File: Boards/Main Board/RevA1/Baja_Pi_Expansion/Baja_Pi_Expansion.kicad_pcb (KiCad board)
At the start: 4 copper layers, 85 x 56 mm, 25 parts, among them J1 Conn_02x10_Counter_Clockwise, J2 Conn_02x12_Counter_Clockwise, J3 Screw_Terminal_01x04, J4 Conn_02x20_Odd_Even, J5 Conn_01x03_Male, J6 Screw_Terminal_01x07, U1 HDSP-7403

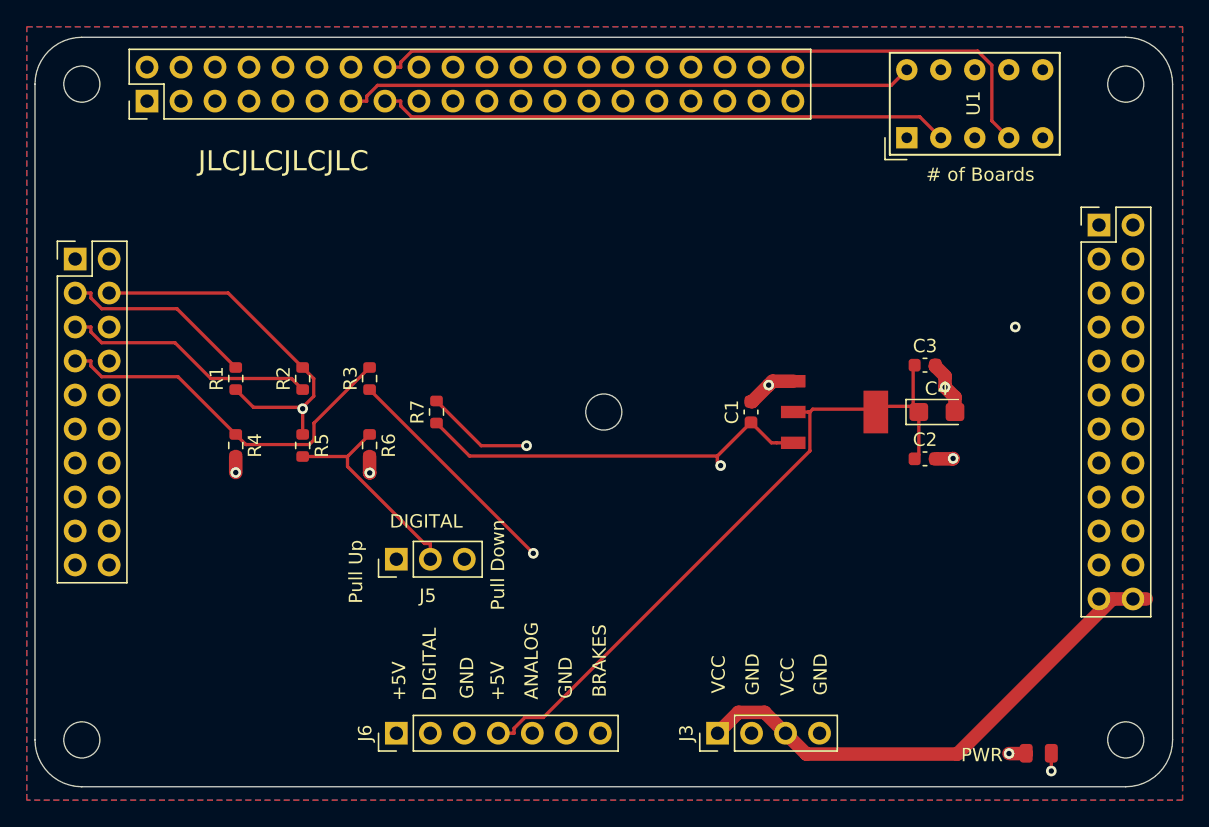
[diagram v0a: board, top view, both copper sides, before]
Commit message: /RevA1 Board Set up For Auto-Routing
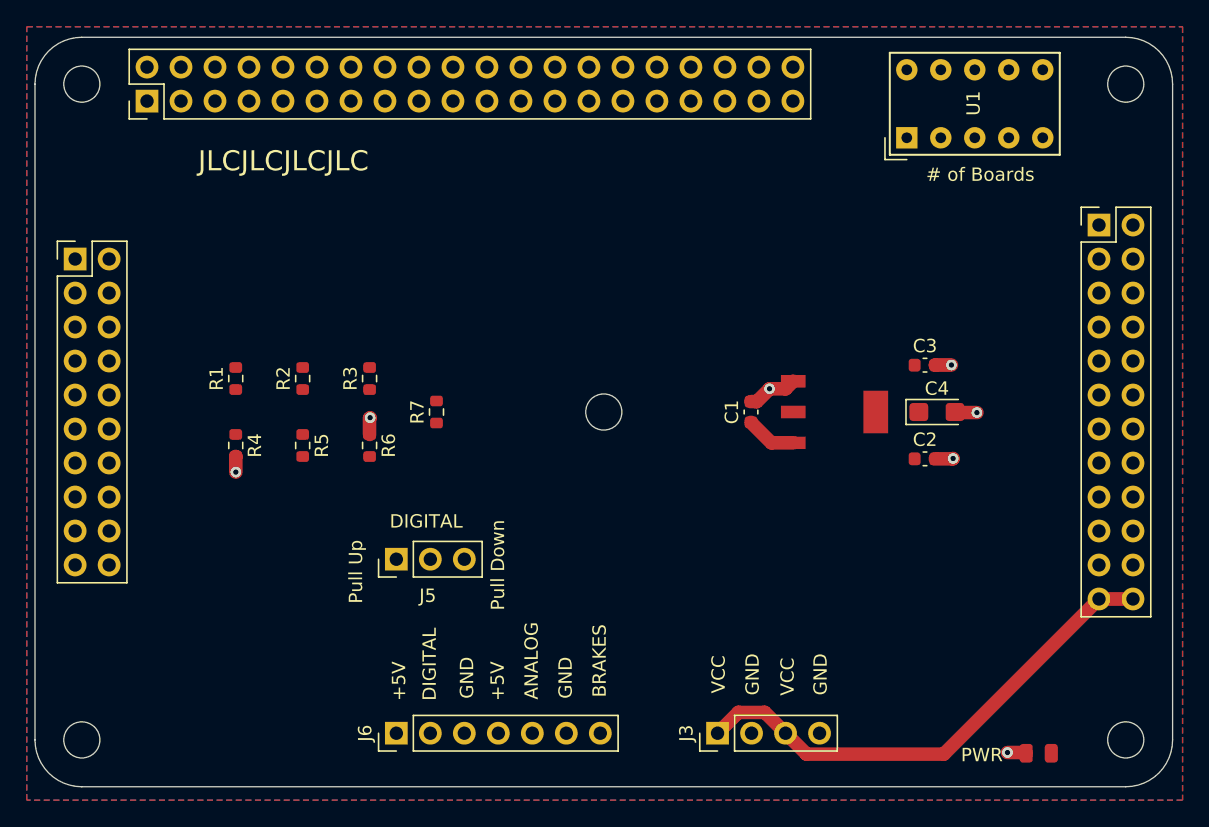
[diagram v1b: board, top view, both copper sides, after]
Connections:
- J5 pad 1: /5v -> Net-(J5-Pad1)
- J5 pad 3: /gnd -> Net-(J5-Pad3)
- R5 pad 1: /5v -> Net-(J5-Pad1)
- R5 pad 2: /dig_in -> /5v
- R6 pad 1: /dig_in -> /gnd
- R6 pad 2: /gnd -> Net-(J5-Pad3)
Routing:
- net /5v: track 137.1 -> 0.00 mm, vias 1 -> 0
- net /dig_in: track 129.4 -> 0.00 mm
- net /analog_in: track 103.6 -> 0.00 mm
- net /gpio8: track 95.0 -> 0.00 mm
- net /gpio7: track 93.5 -> 0.00 mm
- net /gpio6: track 83.3 -> 0.00 mm
- net /gpio11: track 79.5 -> 0.00 mm
- net /miso: track 72.3 -> 0.00 mm
- net /reset: track 64.4 -> 0.00 mm
- net /gpio10: track 58.8 -> 0.00 mm
- net Net-(D1-Pad2): track 58.7 -> 0.00 mm, vias 2 -> 0
- net /gpio4: track 58.3 -> 0.00 mm
- net /3v3: track 57.5 -> 0.00 mm
- net /gpio9: track 55.6 -> 0.00 mm
- net /spi_ce0: track 53.7 -> 0.00 mm
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
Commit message: Added Gerber Files and Main_Board.xlsx
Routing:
- net /5v: track 0.00 -> 140.7 mm
- net /dig_in: track 0.00 -> 111.5 mm
- net /gpio8: track 0.00 -> 99.1 mm
- net /gpio7: track 0.00 -> 96.3 mm
- net /analog_in: track 0.00 -> 88.4 mm, vias 0 -> 1
- net /gpio6: track 0.00 -> 83.2 mm
- net /gpio11: track 0.00 -> 79.5 mm
- net /gpio1: track 0.00 -> 64.1 mm
- net Net-(D1-Pad2): track 0.00 -> 61.2 mm
- net /reset: track 0.00 -> 59.5 mm
- net /scl: track 0.00 -> 58.3 mm
- net /3v3: track 0.00 -> 57.5 mm
- net /gpio4: track 0.00 -> 56.9 mm
- net /spi_ce1: track 0.00 -> 56.0 mm
- net /gpio9: track 0.00 -> 55.6 mm
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
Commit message: Prepared 3.5mm Spring Connectors for Main Board
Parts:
- J3: footprint Connector_PinHeader_2.54mm:PinHeader_1x04_P2.54mm_Vertical -> Custom Footprints:Spring_4
- J6: footprint Connector_PinHeader_2.54mm:PinHeader_1x07_P2.54mm_Vertical -> Custom Footprints:Spring_7
- moved J5 19.9 mm to (171.1, 120.9)
- moved J6 9.68 mm to (181.9, 113.8), turned to 0 degrees
- moved J3 7.76 mm to (210.1, 114.3), turned to 0 degrees
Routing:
- net /5v: track 140.7 -> 0.00 mm
- net /dig_in: track 111.5 -> 0.00 mm
- net /gpio8: track 99.1 -> 0.00 mm
- net /gpio7: track 96.3 -> 0.00 mm
- net /analog_in: track 88.4 -> 0.00 mm, vias 1 -> 0
- net /gpio6: track 83.2 -> 0.00 mm
- net /gpio11: track 79.5 -> 0.00 mm
- net /gpio1: track 64.1 -> 0.00 mm
- net Net-(D1-Pad2): track 61.2 -> 0.00 mm
- net /reset: track 59.5 -> 0.00 mm
- net /scl: track 58.3 -> 0.00 mm
- net /3v3: track 57.5 -> 0.00 mm
- net /gpio4: track 56.9 -> 0.00 mm
- net /spi_ce1: track 56.0 -> 0.00 mm
- net /gpio9: track 55.6 -> 0.00 mm
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
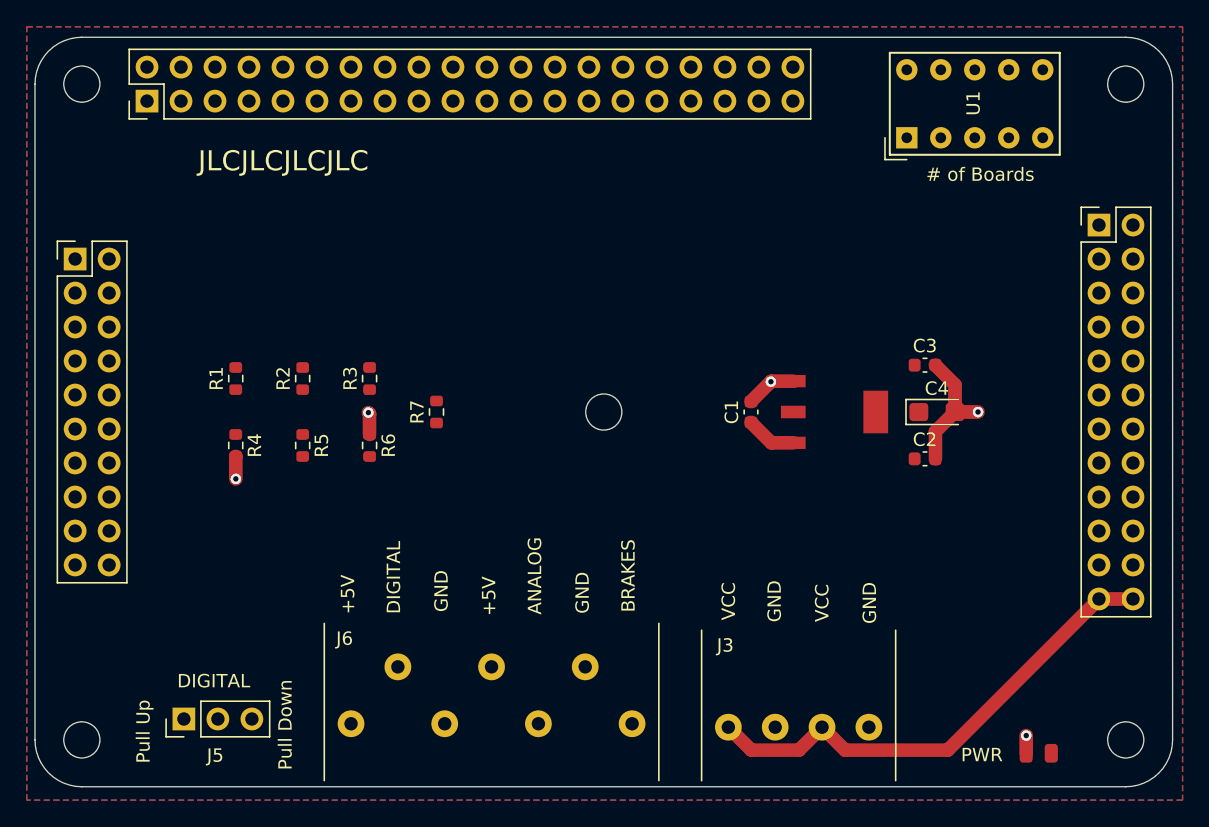
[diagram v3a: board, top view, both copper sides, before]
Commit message: Completed Main Board Routing with 3.5 mm Connectors
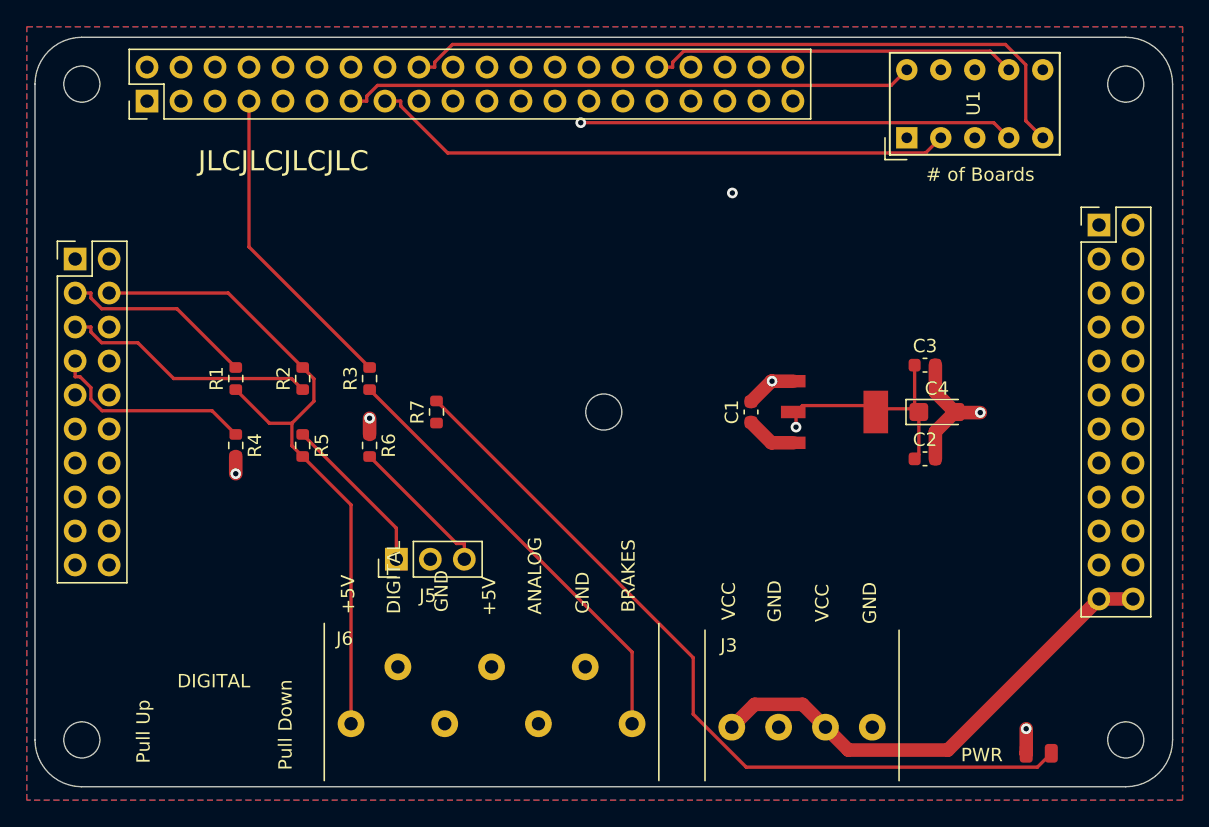
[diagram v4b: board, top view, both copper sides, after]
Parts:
- moved J5 19.9 mm to (187.0, 109.0)
- moved J3 0.25 mm to (210.3, 114.3)
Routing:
- net /5v: track 0.00 -> 133.1 mm, vias 0 -> 1
- net /analog_in: track 0.00 -> 110.0 mm
- net /dig_in: track 0.00 -> 105.5 mm
- net /gpio8: track 0.00 -> 97.5 mm
- net /gpio7: track 0.00 -> 90.9 mm, vias 0 -> 1
- net /gpio6: track 0.00 -> 83.7 mm
- net /gpio11: track 0.00 -> 79.5 mm
- net /gpio1: track 0.00 -> 64.6 mm
- net /miso: track 0.00 -> 64.2 mm
- net /reset: track 0.00 -> 62.7 mm
- net /miso2_pwm: track 0.00 -> 61.0 mm
- net Net-(D1-Pad2): track 0.00 -> 60.2 mm
- net /gpio4: track 0.00 -> 57.6 mm
- net /3v3: track 0.00 -> 57.5 mm
- net /gpio9: track 0.00 -> 55.6 mm
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
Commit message: Completed Main Board Revision A
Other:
- board text removed: "Left to do: Route"
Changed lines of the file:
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@@
   (general
     (thickness 1.6)
-    (drawings 28)
+    (drawings 27)
     (tracks 427)
     (zones 0)
@@
     (effects (font (size 1 1) (thickness 0.15)))
   )
-  (gr_text "Left to do:\nRoute" (at 230.02 130.69) (layer Dwgs.User)
-    (effects (font (size 1 1) (thickness 0.15)))
-  )
